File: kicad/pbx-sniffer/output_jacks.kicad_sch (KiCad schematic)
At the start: 24 parts

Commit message: picked new MCU and updated some part numbers
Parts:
- J25, J26, J27, J28, J29, J30, J31, J32, J33, J34, J35, J36, J37, J38, J39, J40, J41, J42, J43, J44, J45, J46, J47, J48: footprint (none) -> Phones:Molex 0955016649
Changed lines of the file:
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@@
 			)
 		)
-		(property "Footprint" ""
+		(property "Footprint" "Phones:Molex 0955016649"
 			(at 82.55 114.3 0)
 			(effects
@@
 			)
 		)
-		(property "Footprint" ""
+		(property "Footprint" "Phones:Molex 0955016649"
 			(at 204.47 73.66 0)
 			(effects
@@
 			)
 		)
-		(property "Footprint" ""
+		(property "Footprint" "Phones:Molex 0955016649"
 			(at 82.55 33.02 0)
 			(effects
@@
 			)
 		)
-		(property "Footprint" ""
+		(property "Footprint" "Phones:Molex 0955016649"
 			(at 82.55 73.66 0)
 			(effects
@@
 			)
 		)
-		(property "Footprint" ""
+		(property "Footprint" "Phones:Molex 0955016649"
 			(at 82.55 53.34 0)
 			(effects
@@
 			)
 		)
-		(property "Footprint" ""
+		(property "Footprint" "Phones:Molex 0955016649"
 			(at 86.36 93.98 0)
 			(effects
@@
 			)
 		)
-		(property "Footprint" ""
+		(property "Footprint" "Phones:Molex 0955016649"
 			(at 204.47 134.62 0)
 			(effects
@@
 			)
 		)
-		(property "Footprint" ""
+		(property "Footprint" "Phones:Molex 0955016649"
 			(at 86.36 73.66 0)
 			(effects
@@
 			)
 		)
-		(property "Footprint" ""
+		(property "Footprint" "Phones:Molex 0955016649"
 			(at 200.66 114.3 0)
 			(effects
@@
 			)
 		)
-		(property "Footprint" ""
+		(property "Footprint" "Phones:Molex 0955016649"
 			(at 86.36 33.02 0)
 			(effects
@@
 			)
 		)
-		(property "Footprint" ""
+		(property "Footprint" "Phones:Molex 0955016649"
 			(at 200.66 93.98 0)
 			(effects
@@
 			)
 		)
-		(property "Footprint" ""
+		(property "Footprint" "Phones:Molex 0955016649"
 			(at 204.47 114.3 0)
 			(effects
@@
 			)
 		)
-		(property "Footprint" ""
+		(property "Footprint" "Phones:Molex 0955016649"
 			(at 204.47 33.02 0)
 			(effects
@@
 			)
 		)
-		(property "Footprint" ""
+		(property "Footprint" "Phones:Molex 0955016649"
 			(at 204.47 53.34 0)
 			(effects
@@
 			)
 		)
-		(property "Footprint" ""
+		(property "Footprint" "Phones:Molex 0955016649"
 			(at 86.36 114.3 0)
 			(effects
@@
 			)
 		)
-		(property "Footprint" ""
+		(property "Footprint" "Phones:Molex 0955016649"
 			(at 200.66 33.02 0)
 			(effects
@@
 			)
 		)
-		(property "Footprint" ""
+		(property "Footprint" "Phones:Molex 0955016649"
 			(at 86.36 134.62 0)
 			(effects
@@
 			)
 		)
-		(property "Footprint" ""
+		(property "Footprint" "Phones:Molex 0955016649"
 			(at 82.55 93.98 0)
 			(effects
@@
 			)
 		)
-		(property "Footprint" ""
+		(property "Footprint" "Phones:Molex 0955016649"
 			(at 200.66 73.66 0)
 			(effects
@@
 			)
 		)
-		(property "Footprint" ""
+		(property "Footprint" "Phones:Molex 0955016649"
 			(at 200.66 134.62 0)
 			(effects
@@
 			)
 		)
-		(property "Footprint" ""
+		(property "Footprint" "Phones:Molex 0955016649"
 			(at 86.36 53.34 0)
 			(effects
@@
 			)
 		)
-		(property "Footprint" ""
+		(property "Footprint" "Phones:Molex 0955016649"
 			(at 82.55 134.62 0)
 			(effects
@@
 			)
 		)
-		(property "Footprint" ""
+		(property "Footprint" "Phones:Molex 0955016649"
 			(at 200.66 53.34 0)
 			(effects
@@
 			)
 		)
-		(property "Footprint" ""
+		(property "Footprint" "Phones:Molex 0955016649"
 			(at 204.47 93.98 0)
 			(effects

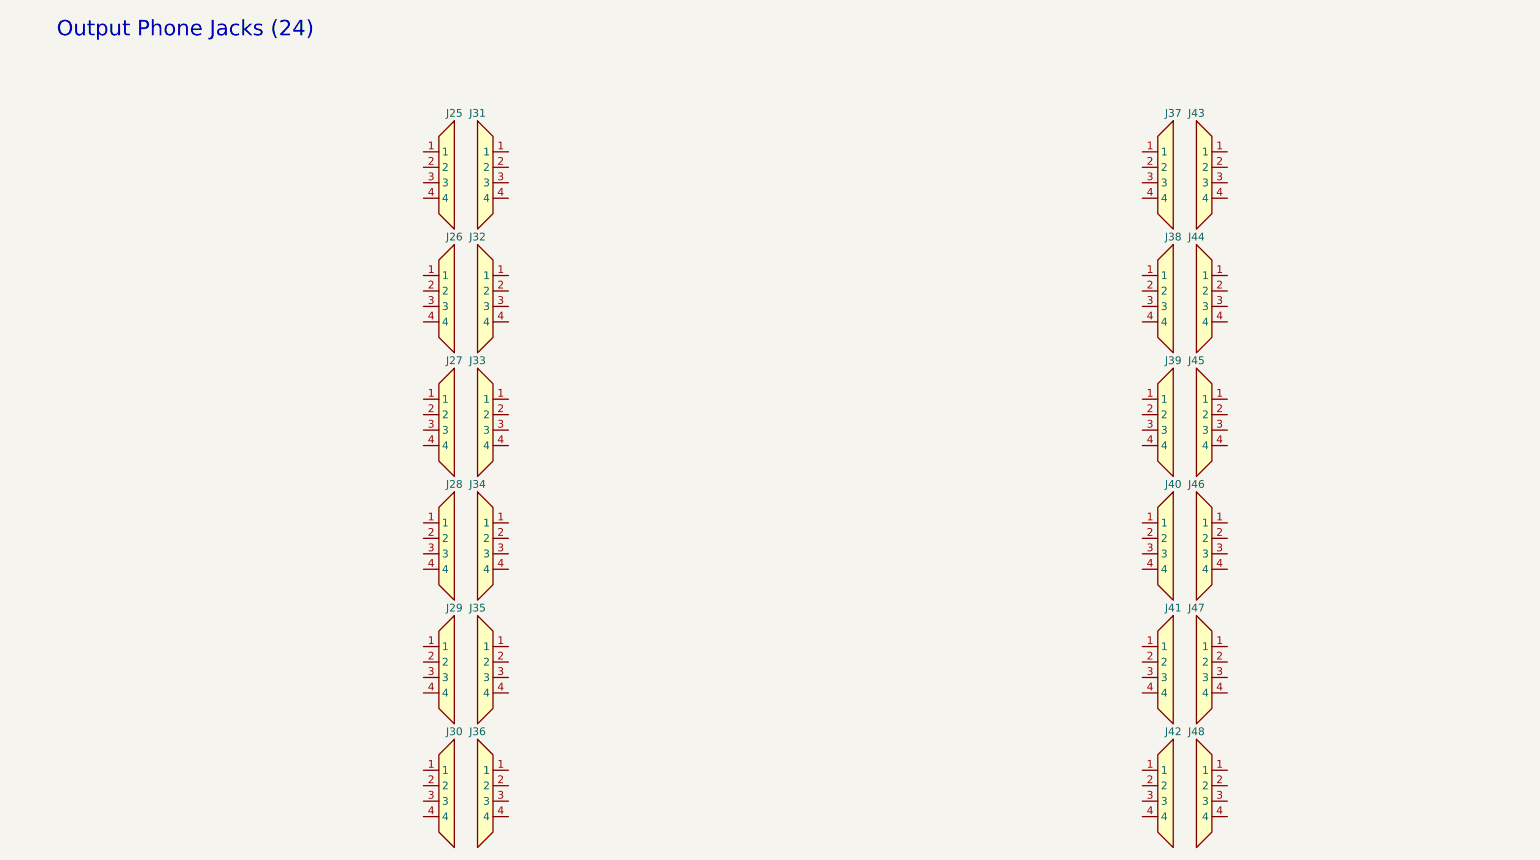
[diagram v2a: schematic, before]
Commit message: working on duplicating adc and control circuits between phone jacks
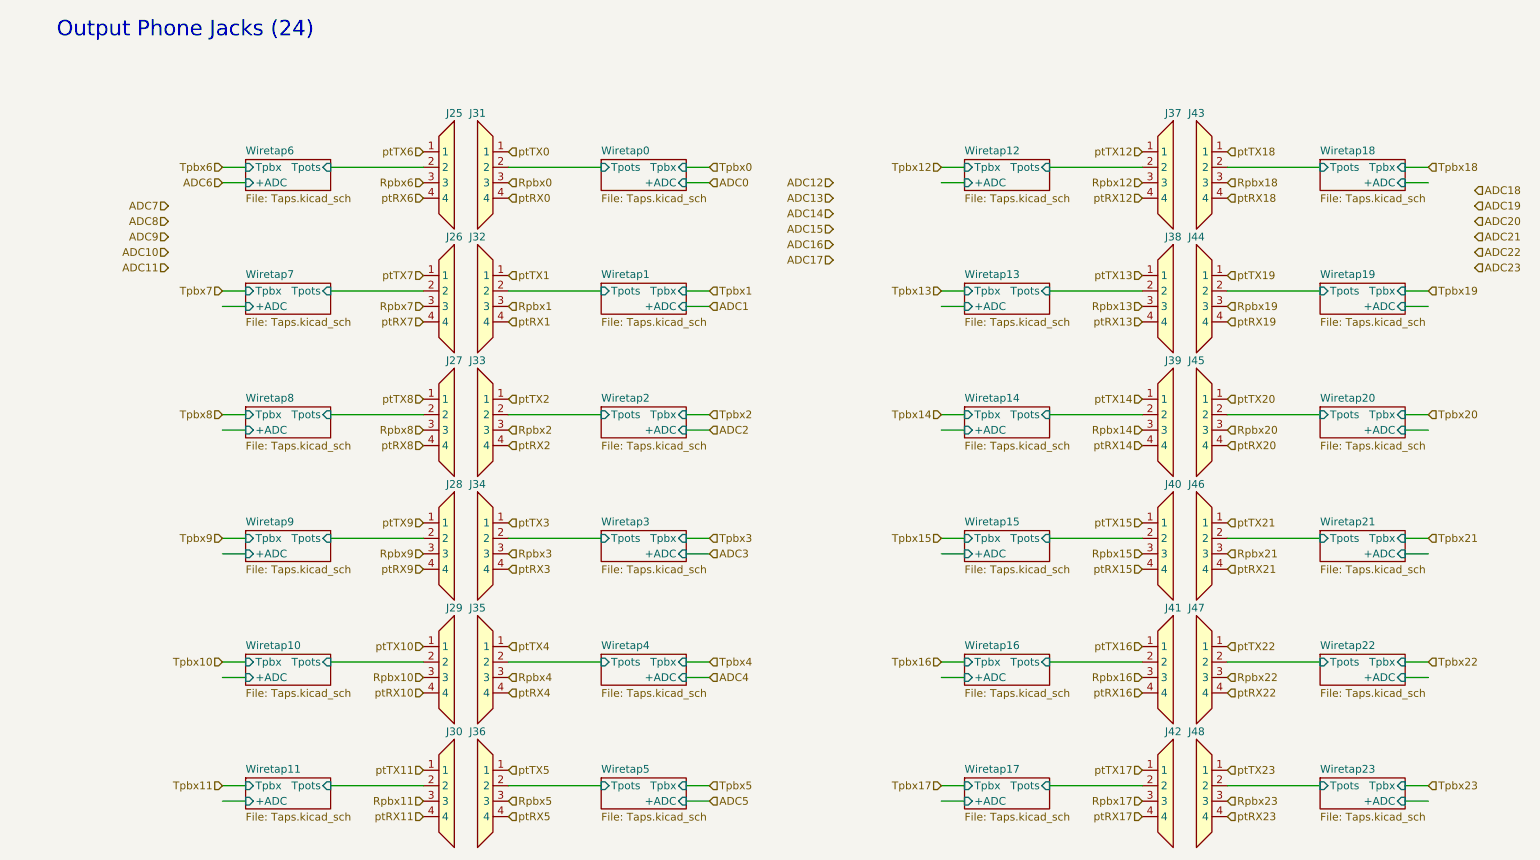
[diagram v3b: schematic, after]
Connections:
- net ptTX10: now reaches J29.1
- net Wiretap10/Tpots: now reaches J29.2
- net Rpbx10: now reaches J29.3
- net ptRX10: now reaches J29.4
- net ptTX20: now reaches J45.1
- net Wiretap20/Tpots: now reaches J45.2
- net Rpbx20: now reaches J45.3
- net ptRX20: now reaches J45.4
- net ptTX6: now reaches J25.1
- net Wiretap6/Tpots: now reaches J25.2
- net Rpbx6: now reaches J25.3
- net ptRX6: now reaches J25.4
- net ptTX8: now reaches J27.1
- net Wiretap8/Tpots: now reaches J27.2
- net Rpbx8: now reaches J27.3
- net ptRX8: now reaches J27.4
- net ptTX7: now reaches J26.1
- net Wiretap7/Tpots: now reaches J26.2
- net Rpbx7: now reaches J26.3
- net ptRX7: now reaches J26.4
- net ptTX3: now reaches J34.1
- net Wiretap3/Tpots: now reaches J34.2
- net Rpbx3: now reaches J34.3
- net ptRX3: now reaches J34.4
- net ptTX23: now reaches J48.1
- net Wiretap23/Tpots: now reaches J48.2
- net Rpbx23: now reaches J48.3
- net ptRX23: now reaches J48.4
- net ptTX2: now reaches J33.1
- net Wiretap2/Tpots: now reaches J33.2
- net Rpbx2: now reaches J33.3
- net ptRX2: now reaches J33.4
- net ptTX16: now reaches J41.1
- net Wiretap16/Tpots: now reaches J41.2
- net Rpbx16: now reaches J41.3
- net ptRX16: now reaches J41.4
- net ptTX0: now reaches J31.1
- net Wiretap0/Tpots: now reaches J31.2
- net Rpbx0: now reaches J31.3
- net ptRX0: now reaches J31.4
- net ptTX15: now reaches J40.1
- net Wiretap15/Tpots: now reaches J40.2
- net Rpbx15: now reaches J40.3
- net ptRX15: now reaches J40.4
- net ptTX22: now reaches J47.1
- net Wiretap22/Tpots: now reaches J47.2
- net Rpbx22: now reaches J47.3
- net ptRX22: now reaches J47.4
- net ptTX18: now reaches J43.1
- net Wiretap18/Tpots: now reaches J43.2
- net Rpbx18: now reaches J43.3
- net ptRX18: now reaches J43.4
- net ptTX19: now reaches J44.1
- net Wiretap19/Tpots: now reaches J44.2
- net Rpbx19: now reaches J44.3
- net ptRX19: now reaches J44.4
- net ptTX4: now reaches J35.1
- net Wiretap4/Tpots: now reaches J35.2
- net Rpbx4: now reaches J35.3
- net ptRX4: now reaches J35.4
- net ptTX12: now reaches J37.1
- net Wiretap12/Tpots: now reaches J37.2
- net Rpbx12: now reaches J37.3
- net ptRX12: now reaches J37.4
- net ptTX5: now reaches J36.1
- net Wiretap5/Tpots: now reaches J36.2
- net Rpbx5: now reaches J36.3
- net ptRX5: now reaches J36.4
- net ptTX9: now reaches J28.1
- net Wiretap9/Tpots: now reaches J28.2
- net Rpbx9: now reaches J28.3
- net ptRX9: now reaches J28.4
- net ptTX14: now reaches J39.1
- net Wiretap14/Tpots: now reaches J39.2
- net Rpbx14: now reaches J39.3
- net ptRX14: now reaches J39.4
- net ptTX17: now reaches J42.1
- net Wiretap17/Tpots: now reaches J42.2
- net Rpbx17: now reaches J42.3
- net ptRX17: now reaches J42.4
- net ptTX1: now reaches J32.1
- net Wiretap1/Tpots: now reaches J32.2
- net Rpbx1: now reaches J32.3
- net ptRX1: now reaches J32.4
- net ptTX11: now reaches J30.1
- net Wiretap11/Tpots: now reaches J30.2
- net Rpbx11: now reaches J30.3
- net ptRX11: now reaches J30.4
- net ptTX13: now reaches J38.1
- net Wiretap13/Tpots: now reaches J38.2
- net Rpbx13: now reaches J38.3
- net ptRX13: now reaches J38.4
- net ptTX21: now reaches J46.1
- net Wiretap21/Tpots: now reaches J46.2
- net Rpbx21: now reaches J46.3
- net ptRX21: now reaches J46.4
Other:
- added sheet Wiretap0 (Taps.kicad_sch)
- added sheet Wiretap1 (Taps.kicad_sch)
- added sheet Wiretap10 (Taps.kicad_sch)
- added sheet Wiretap11 (Taps.kicad_sch)
- added sheet Wiretap12 (Taps.kicad_sch)
- added sheet Wiretap13 (Taps.kicad_sch)
- added sheet Wiretap14 (Taps.kicad_sch)
- added sheet Wiretap15 (Taps.kicad_sch)
- added sheet Wiretap16 (Taps.kicad_sch)
- added sheet Wiretap17 (Taps.kicad_sch)
- added sheet Wiretap18 (Taps.kicad_sch)
- added sheet Wiretap19 (Taps.kicad_sch)
- added sheet Wiretap2 (Taps.kicad_sch)
- added sheet Wiretap20 (Taps.kicad_sch)
- added sheet Wiretap21 (Taps.kicad_sch)
- added sheet Wiretap22 (Taps.kicad_sch)
- added sheet Wiretap23 (Taps.kicad_sch)
- added sheet Wiretap3 (Taps.kicad_sch)
- added sheet Wiretap4 (Taps.kicad_sch)
- added sheet Wiretap5 (Taps.kicad_sch)
- added sheet Wiretap6 (Taps.kicad_sch)
- added sheet Wiretap7 (Taps.kicad_sch)
- added sheet Wiretap8 (Taps.kicad_sch)
- added sheet Wiretap9 (Taps.kicad_sch)

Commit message: finished jack hierachial labels. started putting them on the main sch
(pts
        (xy 45.72 86.36) (xy 59.69 86.36)
    )
    (stroke (width 0) (type default))
    (uuid "8ace12cb-ee30-47b7-8bb3-4f75477c25bd")
)
(wire
    (pts
        (xy 45.72 7.62) (xy 59.69 7.62)
    )
    (stroke (width 0) (type default))
    (uuid "84b70951-4dad-4be3-9586-537893c9e04a")
)
(wire
    (pts
        (xy 45.72 25.4) (xy 59.69 25.4)
    )
    (stroke (width 0) (type default))
    (uuid "a596782f-ae99-45f2-bc6f-3ff7a57a1ee7")
)
(wire
    (pts
        (xy 45.72 22.86) (xy 59.69 22.86)
    )
    (stroke (width 0) (type default))
    (uuid "eaa8a2fd-b211-43aa-899e-a54c76015a70")
)
(wire
    (pts
        (xy 45.72 43.18) (xy 59.69 43.18)
    )
    (stroke (width 0) (type default))
    (uuid "fbbaa87e-b2d5-48b8-b043-e998d4ad25a1")
)
(wire
    (pts
        (xy 45.72 81.28) (xy 59.69 81.28)
    )
    (stroke (width 0) (type default))
    (uuid "74339180-59e3-4aa4-9224-65ca846e8e3c")
)
(wire
    (pts
        (xy 45.72 55.88) (xy 59.69 55.88)
    )
    (stroke (width 0) (type default))
    (uuid "f75722ba-5479-4928-addf-4bcf03d2e5a1")
)
(wire
    (pts
        (xy 45.72 12.7) (xy 59.69 12.7)
    )
    (stroke (width 0) (type default))
    (uuid "b067b129-586d-4458-9293-a7c491fcfe84")
)
(wire
    (pts
        (xy 45.72 45.72) (xy 59.69 45.72)
    )
    (stroke (width 0) (type default))
    (uuid "89d7089e-feae-4ac4-80ce-7609117a820b")
)
(wire
    (pts
        (xy 45.72 27.94) (xy 59.69 27.94)
    )
    (stroke (width 0) (type default))
    (uuid "1f557dbd-c289-4d27-9dcc-8cd8b89deadf")
)
(wire
    (pts
        (xy 45.72 15.24) (xy 59.69 15.24)
    )
    (stroke (width 0) (type default))
    (uuid "be64a9fe-163d-449f-888e-4a585432744b")
)
(wire
    (pts
        (xy 45.72 48.26) (xy 59.69 48.26)
    )
    (stroke (width 0) (type default))
    (uuid "d4da723b-c601-47e4-9bb4-8c723ce5d480")
)
(wire
    (pts
        (xy 45.72 53.34) (xy 59.69 53.34)
    )
    (stroke (width 0) (type default))
    (uuid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
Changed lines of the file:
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@@
 	(hierarchical_label "ADC15"
 		(shape input)
-		(at 144.78 50.8 180)
+		(at 162.56 104.14 180)
 		(effects
 			(font
@@
 	(hierarchical_label "ADC8"
 		(shape input)
-		(at 35.56 49.53 180)
+		(at 44.45 83.82 180)
 		(effects
 			(font
@@
 	(hierarchical_label "ADC17"
 		(shape input)
-		(at 144.78 55.88 180)
+		(at 162.56 144.78 180)
 		(effects
 			(font
@@
 	(hierarchical_label "ADC12"
 		(shape input)
-		(at 144.78 43.18 180)
+		(at 162.56 43.18 180)
 		(effects
 			(font
@@
 	(hierarchical_label "ADC16"
 		(shape input)
-		(at 144.78 53.34 180)
+		(at 162.56 124.46 180)
 		(effects
 			(font
@@
 	(hierarchical_label "ADC22"
 		(shape input)
-		(at 250.19 54.61 0)
+		(at 242.57 124.46 0)
 		(effects
 			(font
@@
 	(hierarchical_label "ADC23"
 		(shape input)
-		(at 250.19 57.15 0)
+		(at 242.57 144.78 0)
 		(effects
 			(font
@@
 	(hierarchical_label "ADC11"
 		(shape input)
-		(at 35.56 57.15 180)
+		(at 44.45 144.78 180)
 		(effects
 			(font
@@
 	(hierarchical_label "ADC19"
 		(shape input)
-		(at 250.19 46.99 0)
+		(at 242.57 63.5 0)
 		(effects
 			(font
@@
 	(hierarchical_label "ADC18"
 		(shape input)
-		(at 250.19 44.45 0)
+		(at 242.57 43.18 0)
 		(effects
 			(font
@@
 	(hierarchical_label "ADC13"
 		(shape input)
-		(at 144.78 45.72 180)
+		(at 162.56 63.5 180)
 		(effects
 			(font
@@
 	(hierarchical_label "ADC21"
 		(shape input)
-		(at 250.19 52.07 0)
+		(at 242.57 104.14 0)
 		(effects
 			(font
@@
 	(hierarchical_label "ADC9"
 		(shape input)
-		(at 35.56 52.07 180)
+		(at 44.45 104.14 180)
 		(effects
 			(font
@@
 	(hierarchical_label "ADC7"
 		(shape input)
-		(at 35.56 46.99 180)
+		(at 44.45 63.5 180)
 		(effects
 			(font
@@
 	(hierarchical_label "ADC14"
 		(shape input)
-		(at 144.78 48.26 180)
+		(at 162.56 83.82 180)
 		(effects
 			(font
@@
 	(hierarchical_label "ADC10"
 		(shape input)
-		(at 35.56 54.61 180)
+		(at 44.45 124.46 180)
 		(effects
 			(font
@@
 	(hierarchical_label "ADC20"
 		(shape input)
-		(at 250.19 49.53 0)
-		(effects
-			(font
+		(at 242.57 83.82 0)
+		(effects
+			(font
